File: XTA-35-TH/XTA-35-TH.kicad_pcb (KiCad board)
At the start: 4 copper layers, 100 x 98.7 mm, 36 parts, among them J1 XTA_Connector, J2 XTA Power, J3 LED, J4 SD0, J5 SD1, J6 Debug, SW1 Config, SW2 Boot Internal, SW3 Reset, U1 74LVC245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

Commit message: Production files. Also added a relief USB connector body after sending for production.
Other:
- outline, holes or cut-outs redrawn
- board text added: "BOOT MENU"
- board text added: "To access the boot menu, eject all floppy disks, then hold down the boot menu while the BIOS is booting from the IntelliDrive. The boot menu can be accessed even if no SD card is present or no operating system is installed."
- board text removed: "VIRTUAL FLOPPY BOOT"

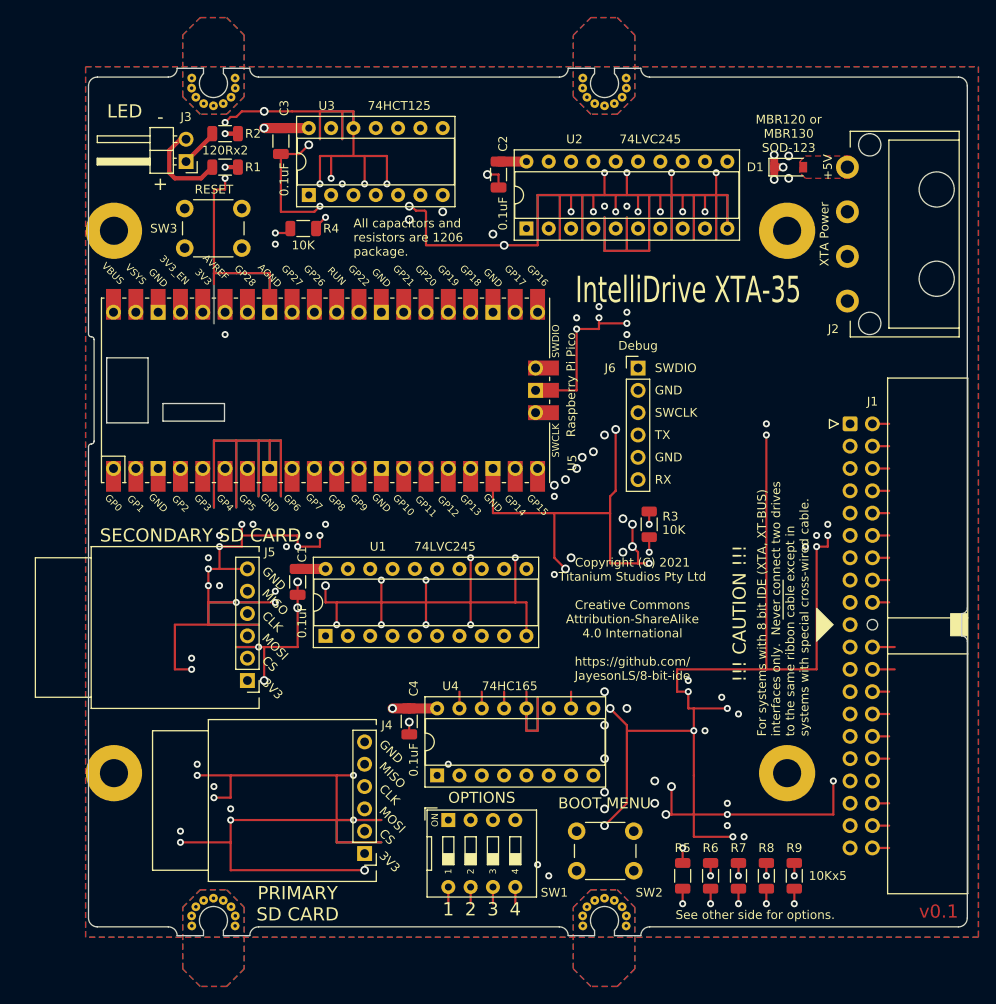
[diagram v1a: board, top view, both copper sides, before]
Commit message: Reorder Pico pins and fix direction of 245's.
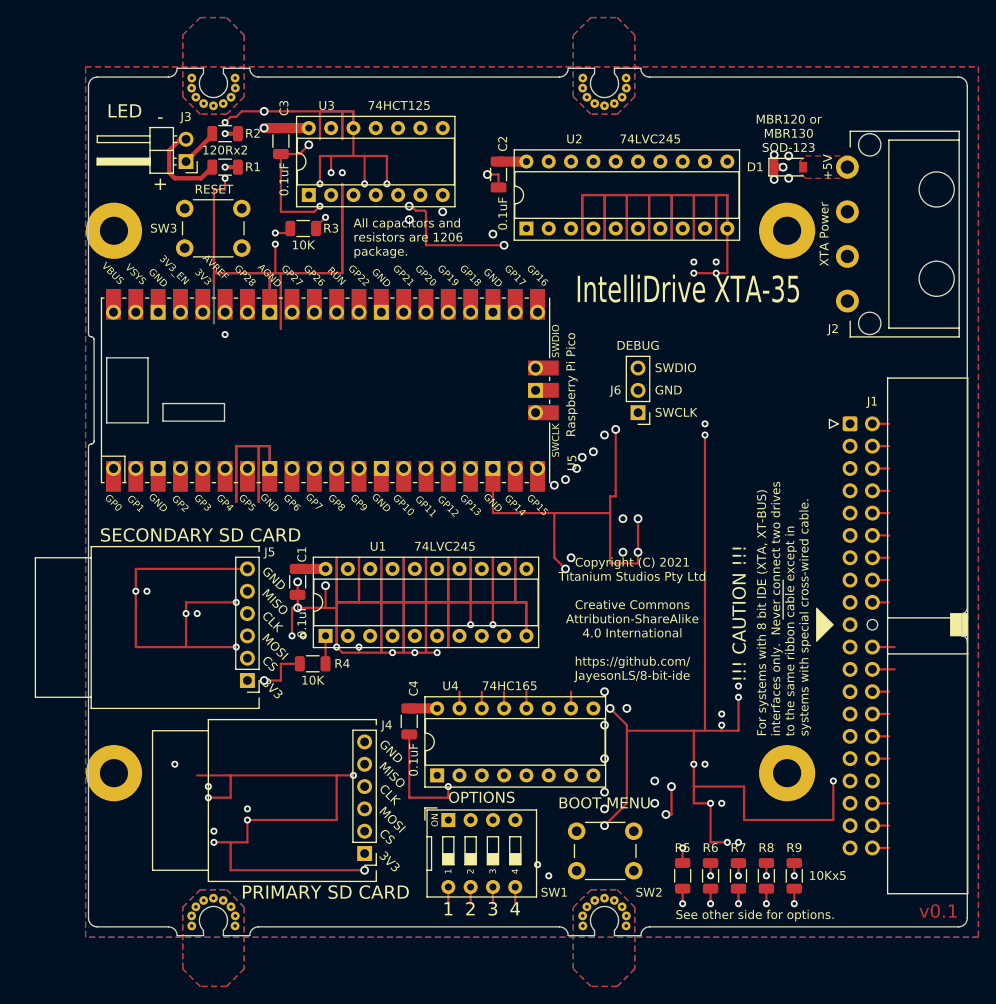
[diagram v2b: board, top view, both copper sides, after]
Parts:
- removed the R3 at (214.0, 82.5)
- added R4: 10K, Resistor_SMD:R_1206_3216Metric, F.Cu at (175.7, 98.4)
- J6: value Debug -> DEBUG; footprint Connector_PinHeader_2.54mm:PinHeader_1x06_P2.54mm_Vertical -> Connector_PinHeader_2.54mm:PinHeader_1x03_P2.54mm_Vertical
- moved J6 5.08 mm to (212.7, 69.8), turned to 180 degrees
- renumbered R4 to R3
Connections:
- net /BOOT_INTERNAL renamed /BOOT_OVERRIDE
- J4 pad 2: CFG_LATCH -> SD0_CS
- J5 pad 2: SD1_CS -> CFG_LATCH
- J6 pad 1: /SWDIO -> /SWCLK
- J6 pad 3: /SWCLK -> /SWDIO
- U1 pad 11: D7_3V3 -> D7
- U1 pad 12: D6_3V3 -> D6
- U1 pad 13: D5_3V3 -> D5
- U1 pad 14: D4_3V3 -> D4
- U1 pad 15: D3_3V3 -> D3
- U1 pad 16: D2_3V3 -> D2
- U1 pad 17: D1_3V3 -> D1
- U1 pad 18: D0_3V3 -> D0
- U1 pad 2: D0 -> D0_3V3
- U1 pad 3: D1 -> D1_3V3
- U1 pad 4: D2 -> D2_3V3
- U1 pad 5: D3 -> D3_3V3
- U1 pad 6: D4 -> D4_3V3
- U1 pad 7: D5 -> D5_3V3
- U1 pad 8: D6 -> D6_3V3
- U1 pad 9: D7 -> D7_3V3
- U2 pad 11: ~IOW~_3V3 -> ~IOW
- U2 pad 12: ~IOR~_3V3 -> ~IOR
- U2 pad 13: ~RESET~_3V3 -> ~CS
- U2 pad 14: ~CS~_3V3 -> AEN
- U2 pad 15: ~DACK~_3V3 -> ~DACK
- U2 pad 16: AEN_3V3 -> ~RESET
- U2 pad 17: A1_3V3 -> A0
- U2 pad 18: A0_3V3 -> A1
- U2 pad 2: A0 -> A1_3V3
- U2 pad 3: A1 -> A0_3V3
- U2 pad 4: AEN -> ~RESET~_3V3
- U2 pad 5: ~DACK -> ~DACK~_3V3
- U2 pad 6: ~CS -> AEN_3V3
- U2 pad 7: ~RESET -> ~CS~_3V3
- U2 pad 8: ~IOR -> ~IOR~_3V3
- U2 pad 9: ~IOW -> ~IOW~_3V3
- U5 pad 1: DBG_RX -> SPI_RX
- U5 pad 10: D3_3V3 -> DATA_DIR
- U5 pad 11: D4_3V3 -> D0_3V3
- U5 pad 12: D5_3V3 -> D1_3V3
- U5 pad 14: D6_3V3 -> D2_3V3
- U5 pad 15: D7_3V3 -> D3_3V3
- U5 pad 16: A0_3V3 -> D4_3V3
- U5 pad 17: A1_3V3 -> D5_3V3
- U5 pad 19: AEN_3V3 -> D6_3V3
- U5 pad 2: CFG_CLK -> SD0_CS
- U5 pad 20: ~DACK~_3V3 -> D7_3V3
- U5 pad 21: SPI_RX -> A0_3V3
- U5 pad 22: ~IOW~_3V3 -> A1_3V3
- U5 pad 24: SPI_SCK -> ~CS~_3V3
- U5 pad 25: SPI_TX -> AEN_3V3
- U5 pad 27: ~RESET~_3V3 -> ~IOW~_3V3
- U5 pad 29: DATA_DIR -> ~DACK~_3V3
- U5 pad 31: ~CS~_3V3 -> ~RESET~_3V3
- U5 pad 4: CFG_LATCH -> SPI_SCK
- U5 pad 5: SD1_CS -> SPI_TX
- U5 pad 6: D0_3V3 -> CFG_LATCH
- U5 pad 7: D1_3V3 -> CFG_CLK
- U5 pad 9: D2_3V3 -> CFG_DATA
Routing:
- net DBG_RX: track 72.3 -> 0.00 mm, vias 1 -> 0
- net CFG_CLK: track 162.4 -> 100.3 mm, vias 2 -> 1
- net SD0_CS: track 0.00 -> 62.1 mm, vias 0 -> 1
- net A0_3V3: track 45.9 -> 11.1 mm
- net SPI_TX: track 91.2 -> 57.3 mm, vias 2 -> 1
- net A1_3V3: track 44.8 -> 11.1 mm
- net DATA_DIR: track 57.9 -> 25.9 mm, vias 2 -> 0
- net SPI_SCK: track 89.7 -> 61.0 mm, vias 1 -> 2
- net SD1_CS: track 28.5 -> 0.00 mm, vias 1 -> 0
- net CFG_DATA: track 31.2 -> 59.5 mm, vias 2 -> 1
- net SPI_RX: track 97.9 -> 70.2 mm
- net ~CS~_3V3: track 52.4 -> 27.8 mm
- net CFG_LATCH: track 74.4 -> 50.5 mm, vias 1 -> 0
- net AEN_3V3: track 46.0 -> 29.1 mm
- net ~RESET: track 36.1 -> 50.6 mm
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
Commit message: Update board and schematic pdf to match latest changes.
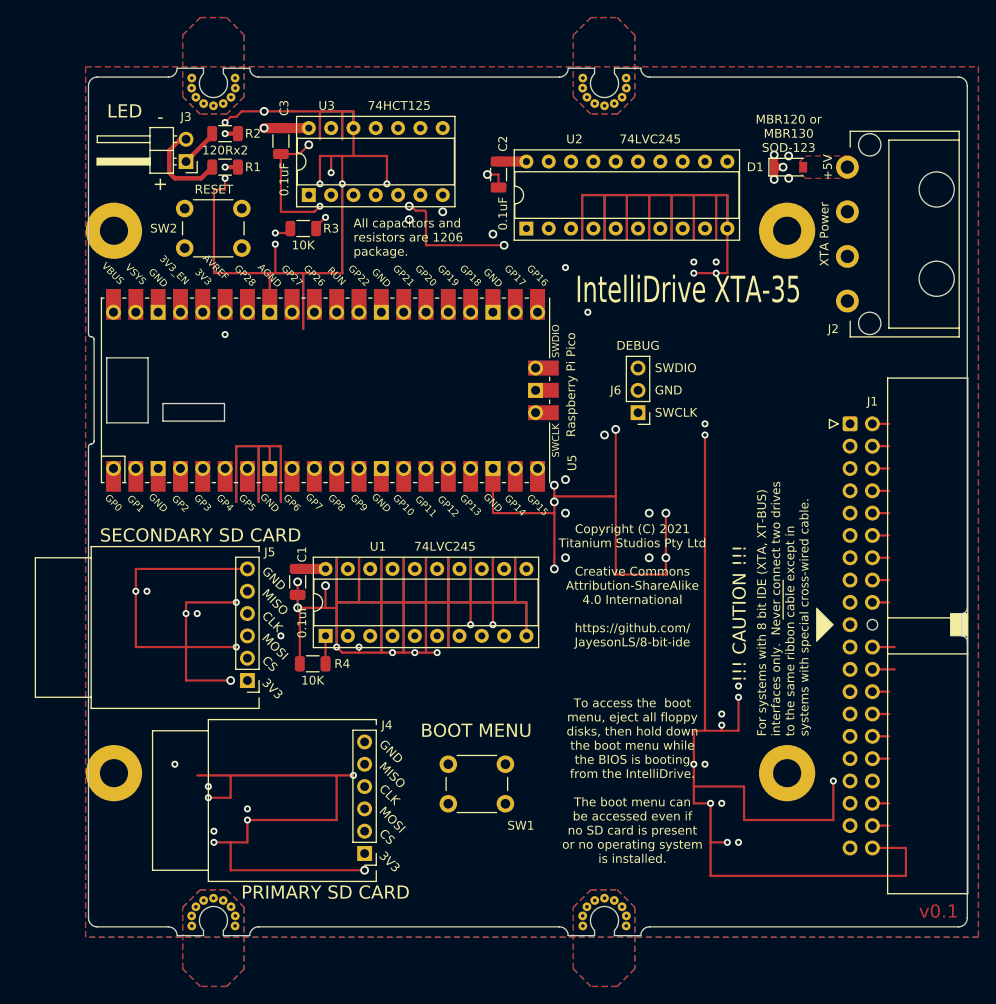
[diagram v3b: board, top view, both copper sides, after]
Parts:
- removed C4: 0.1uF, Capacitor_SMD:C_1206_3216Metric
- removed R5, R6, R7, R8, R9: 10K, Resistor_SMD:R_1206_3216Metric
- removed the SW1 at (191.1, 116.2)
- removed U4: 74HC165, Package_DIP:DIP-16_W7.62mm_Socket
- SW1: renamed from SW2; value Boot Internal -> Boot Override
- moved SW1 16.5 mm to (191.1, 109.9)
- renumbered SW3 to SW2
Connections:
- net CFG_LATCH renamed SD1_CS
- net Net-(SW3-Pad1) renamed /RUN
- net Net-(U5-Pad40) renamed /VBUS
- U3 pad 10: CFG_CLK -> ~DRIVE_ACTIVE~_3V3
- U3 pad 13: CFG_CLK -> ~DRIVE_ACTIVE~_3V3
- U5 pad 10: DATA_DIR -> D1_3V3
- U5 pad 11: D0_3V3 -> D2_3V3
- U5 pad 12: D1_3V3 -> D3_3V3
- U5 pad 14: D2_3V3 -> D4_3V3
- U5 pad 15: D3_3V3 -> D5_3V3
- U5 pad 16: D4_3V3 -> D6_3V3
- U5 pad 17: D5_3V3 -> D7_3V3
- U5 pad 19: D6_3V3 -> ~DACK~_3V3
- U5 pad 20: D7_3V3 -> ~IOR~_3V3
- U5 pad 21: A0_3V3 -> ~IOW~_3V3
- U5 pad 22: A1_3V3 -> ~CS~_3V3
- U5 pad 24: ~CS~_3V3 -> AEN_3V3
- U5 pad 25: AEN_3V3 -> A0_3V3
- U5 pad 26: ~IOR~_3V3 -> A1_3V3
- U5 pad 27: ~IOW~_3V3 -> ~DRQ~_3V3
- U5 pad 29: ~DACK~_3V3 -> ~IRQ~_3V3
- U5 pad 31: ~RESET~_3V3 -> ~DRIVE_ACTIVE~_3V3
- U5 pad 32: ~IRQ~_3V3 -> DATA_DIR
- U5 pad 34: ~DRQ~_3V3 -> ~RESET~_3V3
- U5 pad 7: CFG_CLK -> /BOOT_OVERRIDE
- U5 pad 9: CFG_DATA -> D0_3V3
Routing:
- net CFG_CLK: track 100.3 -> 0.00 mm, vias 1 -> 0
- net +3V3: track 255.5 -> 175.9 mm, vias 23 -> 9
- net CFG_DATA: track 59.5 -> 0.00 mm, vias 1 -> 0
- net /RESET_INVERT: track 47.7 -> 0.00 mm, vias 2 -> 0
- net /IRQ_SELECT: track 41.7 -> 0.00 mm, vias 2 -> 0
- net /OPTION_4: track 37.7 -> 0.00 mm, vias 1 -> 0
- net /OPTION_3: track 37.1 -> 0.00 mm, vias 1 -> 0
- net ~DRIVE_ACTIVE~_3V3: track 0.00 -> 34.8 mm
- net SD1_CS: track 50.5 -> 25.0 mm
- net ~IOW~_3V3: track 46.2 -> 28.3 mm
- net DATA_DIR: track 25.9 -> 43.7 mm
- net ~DRQ~_3V3: track 17.0 -> 28.6 mm
- net GND: track 909.1 -> 899.4 mm, vias 56 -> 50
- net /BOOT_OVERRIDE: track 45.7 -> 54.9 mm
- net A1_3V3: track 11.1 -> 20.2 mm
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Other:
- board text removed: "1"
- board text removed: "10Kx5"
- board text removed: "2"
- board text removed: "3"
- board text removed: "4"
- board text removed: "OPTIONS"
- board text removed: "OPTIONS: 1 IRQ selection. OFF: Default. ON: Alternate Requires mainboard / interface card IRQ to be set to match. 2. Reset level. OFF: Low, ON: High 3. Reserved for future use. 4. Reserved for future use."
- board text removed: "See other side for options."

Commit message: More pin reassignments.
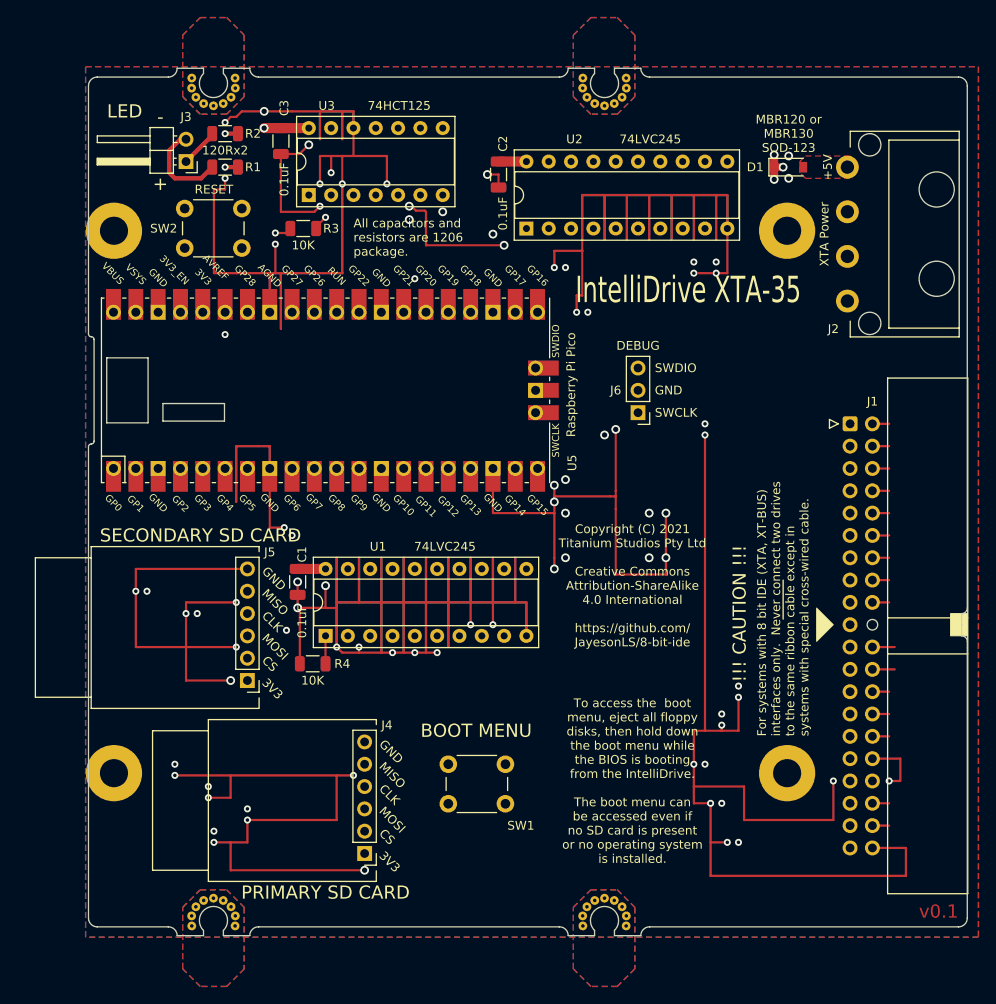
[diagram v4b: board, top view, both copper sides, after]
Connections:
- U5 pad 10: D1_3V3 -> D2_3V3
- U5 pad 11: D2_3V3 -> D3_3V3
- U5 pad 12: D3_3V3 -> D4_3V3
- U5 pad 14: D4_3V3 -> D5_3V3
- U5 pad 15: D5_3V3 -> D6_3V3
- U5 pad 16: D6_3V3 -> D7_3V3
- U5 pad 17: D7_3V3 -> DATA_DIR
- U5 pad 31: ~DRIVE_ACTIVE~_3V3 -> /BOOT_OVERRIDE
- U5 pad 32: DATA_DIR -> ~DRIVE_ACTIVE~_3V3
- U5 pad 7: /BOOT_OVERRIDE -> D0_3V3
- U5 pad 9: D0_3V3 -> D1_3V3
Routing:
- net /BOOT_OVERRIDE: track 54.9 -> 102.7 mm, vias 1 -> 2
- net D0_3V3: track 22.7 -> 27.8 mm
- net D4_3V3: track 21.7 -> 25.3 mm
- net ~DRQ~_3V3: track 28.6 -> 32.2 mm
- net D1_3V3: track 22.7 -> 25.3 mm
- net D2_3V3: track 22.7 -> 25.3 mm
- net D3_3V3: track 22.7 -> 25.3 mm
- net GND: track 899.4 -> 901.4 mm, vias 50 -> 55
- net ~DRIVE_ACTIVE~_3V3: track 34.8 -> 35.9 mm
- net D7_3V3: track 21.7 -> 22.7 mm
- net D6_3V3: track 21.7 -> 22.7 mm
- net D5_3V3: track 21.7 -> 22.7 mm
- net ~DRIVE_ACTIVE: track 144.0 -> 144.5 mm
- net SD1_CS: track 25.0 -> 25.5 mm
- net DATA_DIR: vias 0 -> 1

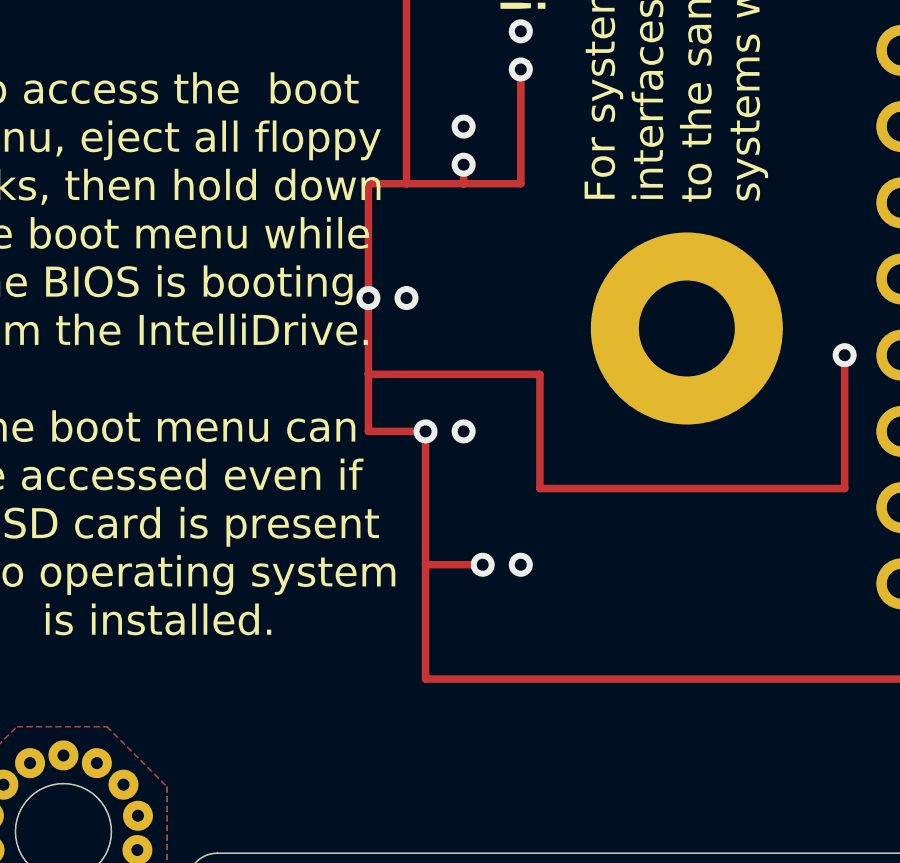
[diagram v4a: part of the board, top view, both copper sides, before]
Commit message: Swap A0/A1 pin assignments.
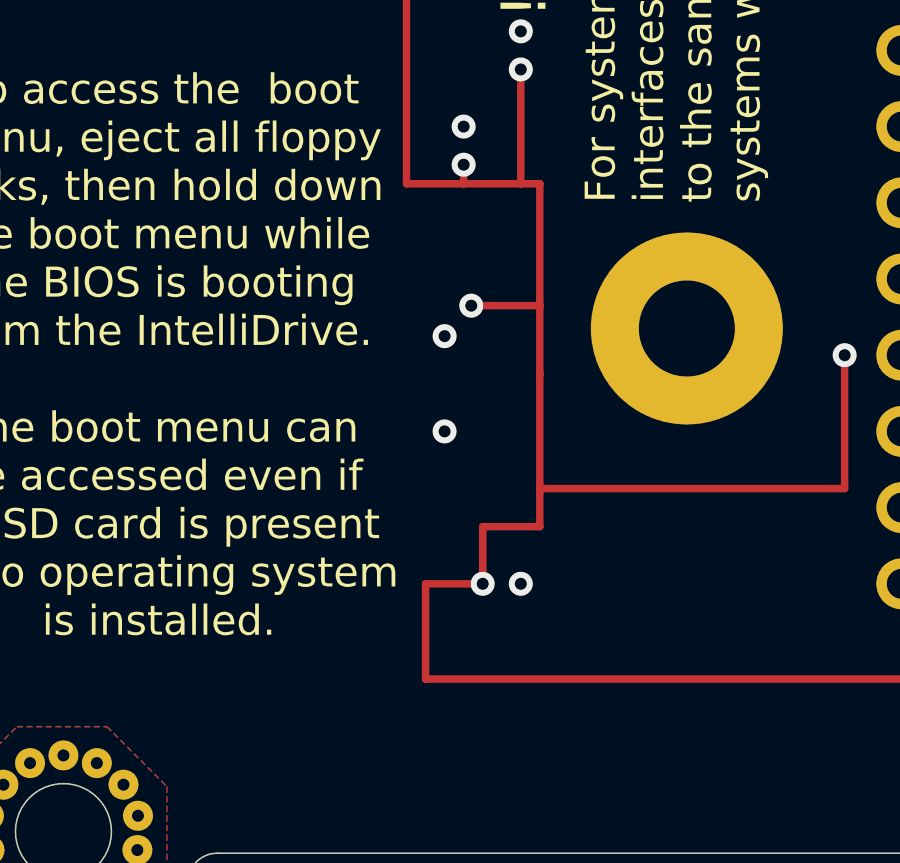
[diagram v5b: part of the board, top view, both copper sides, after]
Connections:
- U2 pad 17: A0 -> A1
- U2 pad 18: A1 -> A0
- U2 pad 2: A1_3V3 -> A0_3V3
- U2 pad 3: A0_3V3 -> A1_3V3
- U5 pad 25: A0_3V3 -> A1_3V3
- U5 pad 26: A1_3V3 -> A0_3V3
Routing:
- net GND: track 901.4 -> 893.6 mm, vias 55 -> 54
- net A0: track 96.3 -> 97.7 mm
- net A1: track 95.3 -> 94.3 mm

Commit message: Add pullup resistors to ~IRQ and ~DRQ.
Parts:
- added R5: 10K, Resistor_SMD:R_1206_3216Metric, F.Cu at (144.1, 39.4)
- added R6: 10K, Resistor_SMD:R_1206_3216Metric, F.Cu at (144.1, 42.7)

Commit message: Change pinout again.
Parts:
- moved R5 46.8 mm to (189.2, 52.1), turned to 270 degrees
- moved R6 42.3 mm to (185.4, 52.1), turned to 270 degrees
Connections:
- net /BOOT_OVERRIDE renamed /~BOOT_OVERRIDE
- U2 pad 17: A1 -> A0
- U2 pad 18: A0 -> A1
- U2 pad 2: A0_3V3 -> A1_3V3
- U2 pad 3: A1_3V3 -> A0_3V3
- U5 pad 17: DATA_DIR -> ~DACK~_3V3
- U5 pad 19: ~DACK~_3V3 -> ~IOW~_3V3
- U5 pad 20: ~IOR~_3V3 -> A0_3V3
- U5 pad 21: ~IOW~_3V3 -> A1_3V3
- U5 pad 25: A1_3V3 -> ~IOR~_3V3
- U5 pad 26: A0_3V3 -> ~DRQ~_3V3
- U5 pad 27: ~DRQ~_3V3 -> ~IRQ~_3V3
- U5 pad 29: ~IRQ~_3V3 -> DATA_DIR
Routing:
- net GND: track 893.6 -> 973.8 mm, vias 54 -> 58
- net /~BOOT_OVERRIDE: track 102.7 -> 86.9 mm
- net ~IOW~_3V3: track 28.3 -> 42.2 mm, vias 0 -> 1
- net A0_3V3: track 19.8 -> 32.7 mm
- net ~DRQ~_3V3: track 32.2 -> 42.9 mm, vias 0 -> 1
- net ~IRQ~_3V3: track 14.1 -> 24.1 mm
- net A1_3V3: track 20.0 -> 10.1 mm
- net +3V3: track 175.9 -> 183.2 mm, vias 9 -> 10
- net ~DACK~_3V3: track 35.4 -> 41.0 mm
- net A1: track 94.3 -> 98.3 mm
- net DATA_DIR: track 43.7 -> 47.3 mm, vias 1 -> 2
- net ~IOR~_3V3: track 35.6 -> 33.8 mm, vias 1 -> 0
- net /RUN: track 32.5 -> 33.7 mm, vias 1 -> 0
- net ~RESET~_3V3: track 44.4 -> 45.5 mm

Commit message: Update board.
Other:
- board text added: "Created by Jayeson Lee-Steere https://github.com/ JayesonLS/8-bit-ide"
- board text removed: "Copyright (C) 2021 Titanium Studios Pty Ltd Creative Commons Attribution-ShareAlike 4.0 International https://github.com/ JayesonLS/8-bit-ide"
